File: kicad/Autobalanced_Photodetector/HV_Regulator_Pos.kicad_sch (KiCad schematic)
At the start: 0 parts

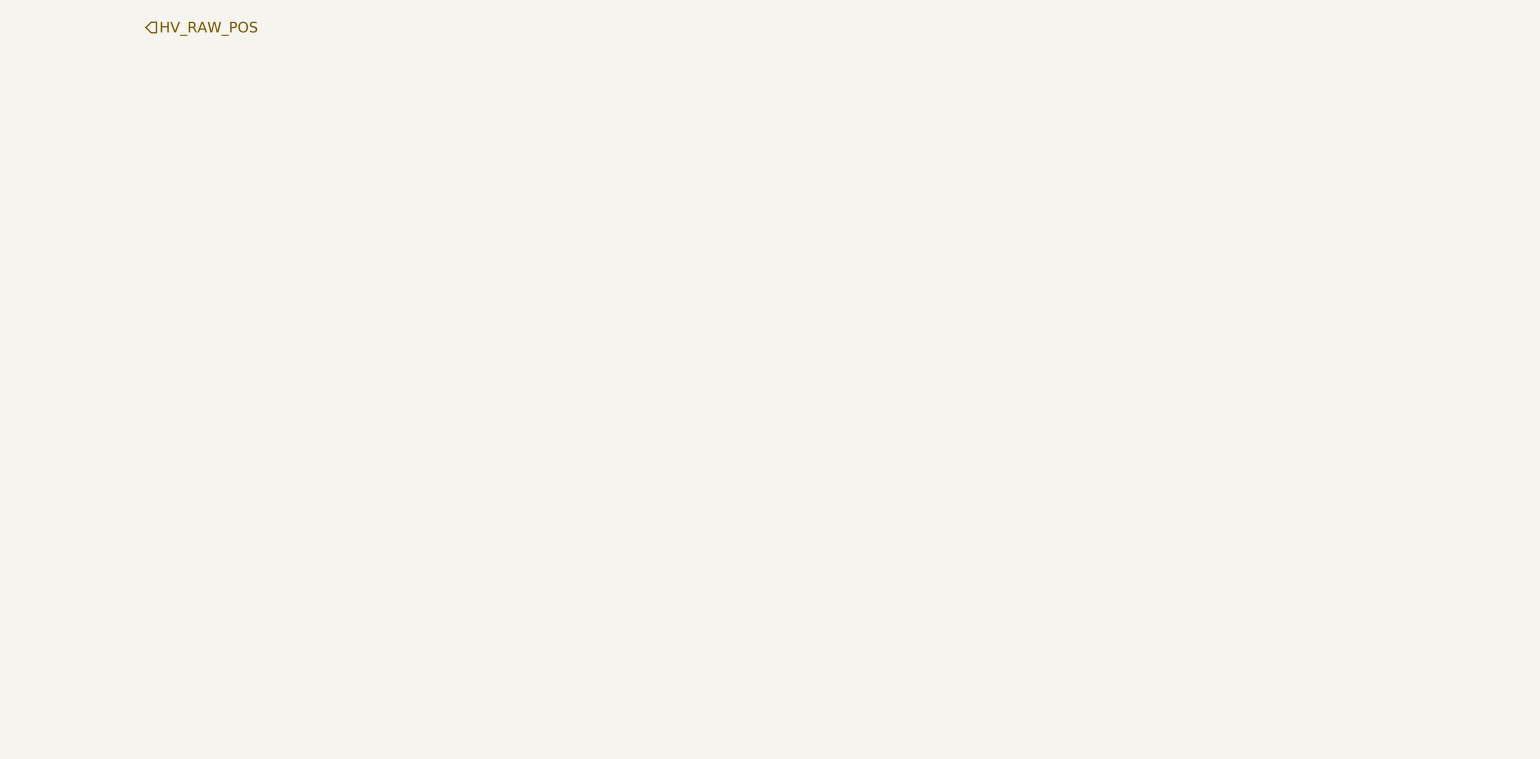
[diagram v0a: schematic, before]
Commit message: feat(kicad): add HV regulators and reference control
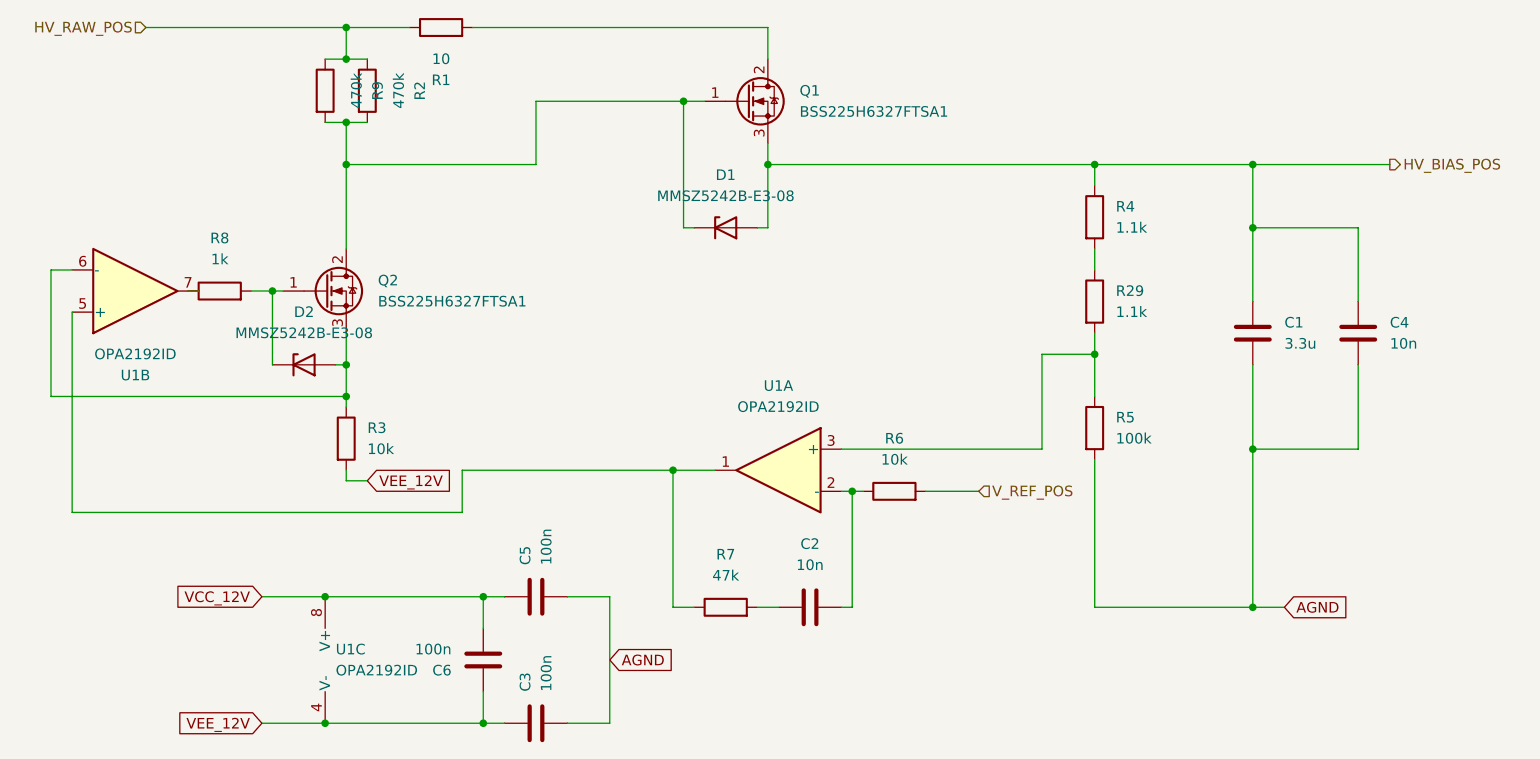
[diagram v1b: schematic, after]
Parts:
- added C1: 3.3u, Capacitor_THT:C_Rect_L29.0mm_W12.2mm_P27.50mm_MKT, symbol Device:C
- added C2: 10n, Capacitor_SMD:C_0805_2012Metric, symbol Device:C
- added C3, C5, C6: 100n, Capacitor_SMD:C_0805_2012Metric, symbol Device:C
- added C4: 10n, Capacitor_SMD:C_1206_3216Metric, symbol Device:C
- added D1, D2: MMSZ5242B-E3-08, Diode_SMD:D_SOD-123, symbol Device:D_Zener
- added Q1, Q2: BSS225H6327FTSA1, Package_TO_SOT_SMD:SOT-89-3, symbol Device:Q_NMOS_GDS
- added R1: 10, Resistor_SMD:R_0805_2012Metric, symbol Device:R
- added R2, R9: 470k, Resistor_SMD:R_1206_3216Metric, symbol Device:R
- added R29, R4: 1.1k, Resistor_SMD:R_0805_2012Metric, symbol Device:R
- added R3, R6: 10k, Resistor_SMD:R_0805_2012Metric, symbol Device:R
- added R5: 100k, Resistor_SMD:R_0805_2012Metric, symbol Device:R
- added R7: 47k, Resistor_SMD:R_0805_2012Metric, symbol Device:R
- added R8: 1k, Resistor_SMD:R_0805_2012Metric, symbol Device:R
- added U1: OPA2192ID, Package_SO:SOIC-8_3.9x4.9mm_P1.27mm, symbol Amplifier_Operational:LM358
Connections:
- net HV_RAW_POS: now also R1.1, R2.1, R9.1
- new net: D1.1 (K), Q1.1 (G), Q2.2 (D), R2.2, R9.2
- new net: R7.1, U1.1, U1.5 (+)
- new net: C2.1, R7.2
- new net: D2.1 (K), Q2.1 (G), R8.2
- new net: D2.2 (A), Q2.3 (S), R3.1, U1.6 (-)
- new net: Q1.2 (D), R1.2
- new net: R29.1, R4.2
- new net: R29.2, R5.1, U1.3 (+)
- new net: C2.2, R6.1, U1.2 (-)
- new net: R8.1, U1.7
- new net AGND: C1.2, C3.2, C4.2, C5.2, R5.2
- new net HV_BIAS_POS: C1.1, C4.1, D1.2 (A), Q1.3 (S), R4.1
- new net VCC_12V: C5.1, C6.2, U1.8 (V+)
- new net VEE_12V: C3.1, C6.1, R3.2, U1.4 (V-)
- new net V_REF_POS: R6.2
